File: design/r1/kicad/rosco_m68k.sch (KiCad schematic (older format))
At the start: 0 parts

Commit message: Initial cleanup
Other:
- note added: "1"
- note added: "Copyright ©2019-2020 Ross Bamford and Contributors.\nOpen Source Hardware licenced under CERN Open Hardware Licence. \nSee https://github.com/roscopeco/rosco_m68k/blob/master/LICENCE.hardware.txt\nOSHWA UK000006 (https://certification.oshwa.org/uk000006.html)\n"
- note added: "ROSCO_M68K GENERAL PURPOSE MC68000 COMPUTER"
- note removed: "2020-02-25\nAddress and data busses are routed through the hierarchical schematic.\nThe Control bus is still routed via global labels, because separately named\nsignals in busses are not implemented yet (Expected in KiCad V6)\n\nBecause the Controll bus still uses global labels, all the blue bus lines of\nthat bus is just eye candy. KiCad just relies on the global labels.\n\n"
- note removed: "2020-02-25\nAfter all the changes I made (and intermediate) I checked the generated \nconnectivity from the schematic with the PCB.\nI have not touched the PCB (after automatic conversion) and DRC does not \ngive errors or unrouted connections, which almost guarantees I did not add\nerrors to the schematic."
- note removed: "2020-02-25\nDouble click to enther a Hierarchical sheet.\n(RMB & select from sub menu to turn back)."
- note removed: "2020-02-25\nERC in EEschem still generates a bunch of errors.\nThese errors are from faults in symbols, for example 2 ouput pins of different IC's connected together."
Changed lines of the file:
@@
 	9300 3700 3400 3700
 Connection ~ 3400 3700
-Text Notes 3400 4850 0    50   ~ 0
-2020-02-25\nAddress and data busses are routed through the hierarchical schematic.\nThe Control bus is still routed via global labels, because separately named\nsignals in busses are not implemented yet (Expected in KiCad V6)\n\nBecause the Controll bus still uses global labels, all the blue bus lines of\nthat bus is just eye candy. KiCad just relies on the global labels.\n\n
-Text Notes 2750 5350 0    50   ~ 0
-2020-02-25\nERC in EEschem still generates a bunch of errors.\nThese errors are from faults in symbols, for example 2 ouput pins of different IC's connected together.
-Text Notes 3250 2050 0    50   ~ 0
-2020-02-25\nDouble click to enther a Hierarchical sheet.\n(RMB & select from sub menu to turn back).
-Text Notes 3500 7400 0    50   ~ 0
-2020-02-25\nAfter all the changes I made (and intermediate) I checked the generated \nconnectivity from the schematic with the PCB.\nI have not touched the PCB (after automatic conversion) and DRC does not \ngive errors or unrouted connections, which almost guarantees I did not add\nerrors to the schematic.
+Text Notes 7000 6950 0    59   ~ 0
+Copyright ©2019-2020 Ross Bamford and Contributors.\nOpen Source Hardware licenced under CERN Open Hardware Licence. \nSee https://github.com/roscopeco/rosco_m68k/blob/master/LICENCE.hardware.txt\nOSHWA UK000006 (https://certification.oshwa.org/uk000006.html)\n
+Text Notes 7350 7500 0    59   ~ 0
+ROSCO_M68K GENERAL PURPOSE MC68000 COMPUTER
+Text Notes 10600 7650 0    59   ~ 0
+1
 $EndSCHEMATC

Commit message: Cleanup first pass
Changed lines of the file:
@@
 $Descr A4 11693 8268
 encoding utf-8
-Sheet 1 7
+Sheet 1 6
 Title ""
 Date "2020-02-25"
@@
 F3 "A[1..23]" I L 9750 2850 50
 $EndSheet
-$Sheet
-S 1400 6100 500  150
-U 5E53BCCF
-F0 "Unused" 50
-F1 "Unused.sch" 50
-$EndSheet
 Text Label 1250 2500 2    50   ~ 0

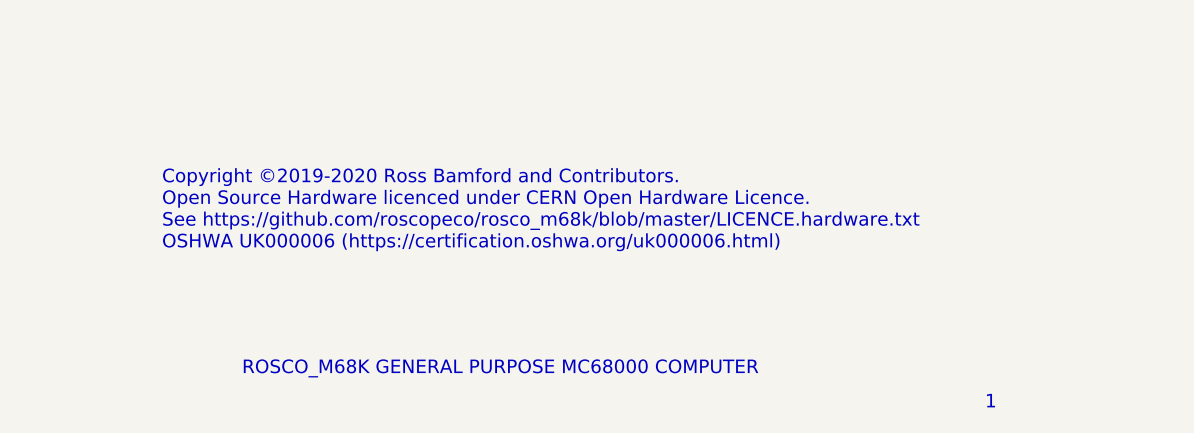
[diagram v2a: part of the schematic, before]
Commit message: Fix #18 and apply suggestions from #17
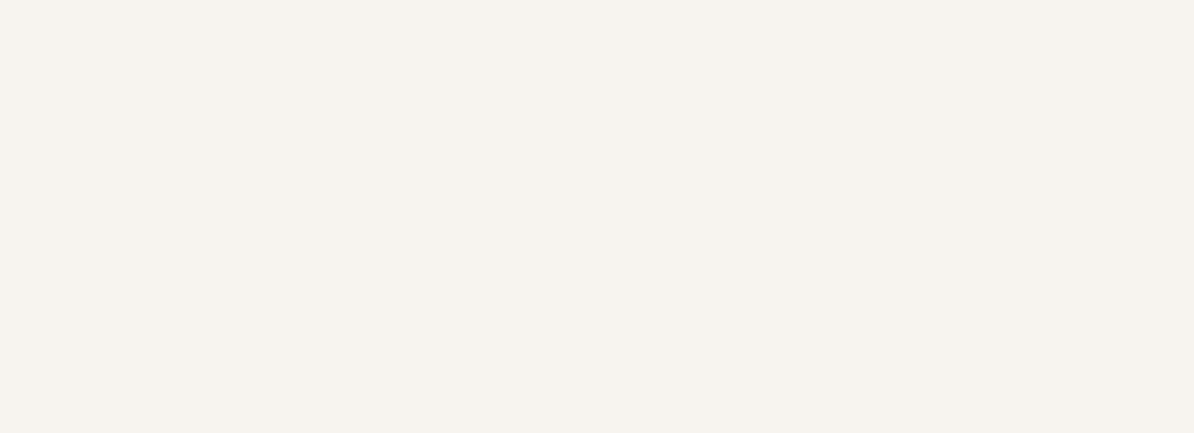
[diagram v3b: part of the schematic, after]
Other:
- note removed: "1"
- note removed: "Copyright ©2019-2020 Ross Bamford and Contributors.\nOpen Source Hardware licenced under CERN Open Hardware Licence. \nSee https://github.com/roscopeco/rosco_m68k/blob/master/LICENCE.hardware.txt\nOSHWA UK000006 (https://certification.oshwa.org/uk000006.html)\n"
- note removed: "ROSCO_M68K GENERAL PURPOSE MC68000 COMPUTER"
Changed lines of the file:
@@
 encoding utf-8
 Sheet 1 6
-Title ""
+Title "ROSCO_M68K GENERAL PURPOSE MC68010 COMPUTER"
 Date "2020-02-25"
-Rev ""
+Rev "1"
 Comp ""
-Comment1 ""
-Comment2 ""
-Comment3 ""
-Comment4 ""
+Comment1 "OSHWA UK000006 (https://certification.oshwa.org/uk000006.html)"
+Comment2 "See https://github.com/roscopeco/rosco_m68k/blob/master/LICENCE.hardware.txt"
+Comment3 "Open Source Hardware licenced under CERN Open Hardware Licence"
+Comment4 "Copyright 2019-2020 Ross Bamford and Contributors"
 $EndDescr
 $Sheet
@@
 	9300 3700 3400 3700
 Connection ~ 3400 3700
-Text Notes 7000 6950 0    59   ~ 0
-Copyright ©2019-2020 Ross Bamford and Contributors.\nOpen Source Hardware licenced under CERN Open Hardware Licence. \nSee https://github.com/roscopeco/rosco_m68k/blob/master/LICENCE.hardware.txt\nOSHWA UK000006 (https://certification.oshwa.org/uk000006.html)\n
-Text Notes 7350 7500 0    59   ~ 0
-ROSCO_M68K GENERAL PURPOSE MC68000 COMPUTER
-Text Notes 10600 7650 0    59   ~ 0
-1
 $EndSCHEMATC
